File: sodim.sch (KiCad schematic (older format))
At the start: 1 part, among them J1 ddr4-sodimm-edge-connector

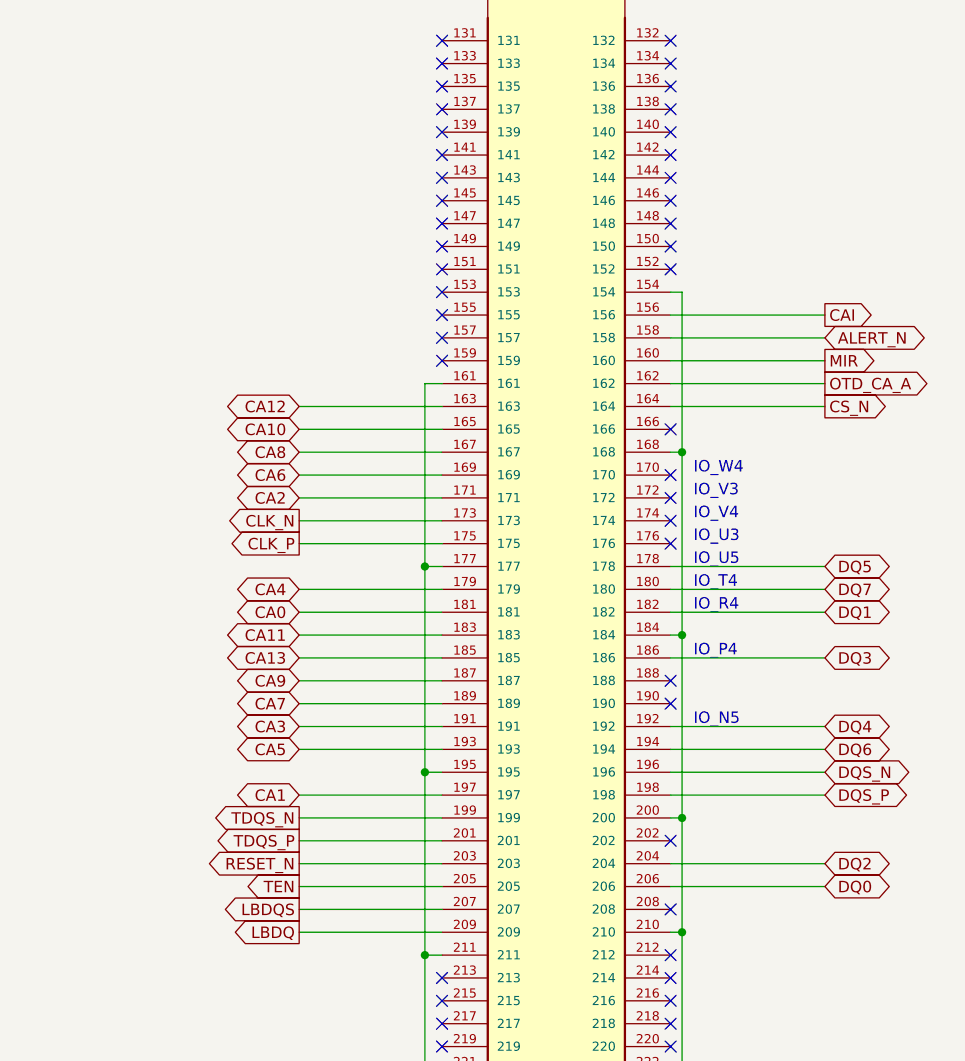
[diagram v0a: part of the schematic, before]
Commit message: Update SODIMM signal assignment
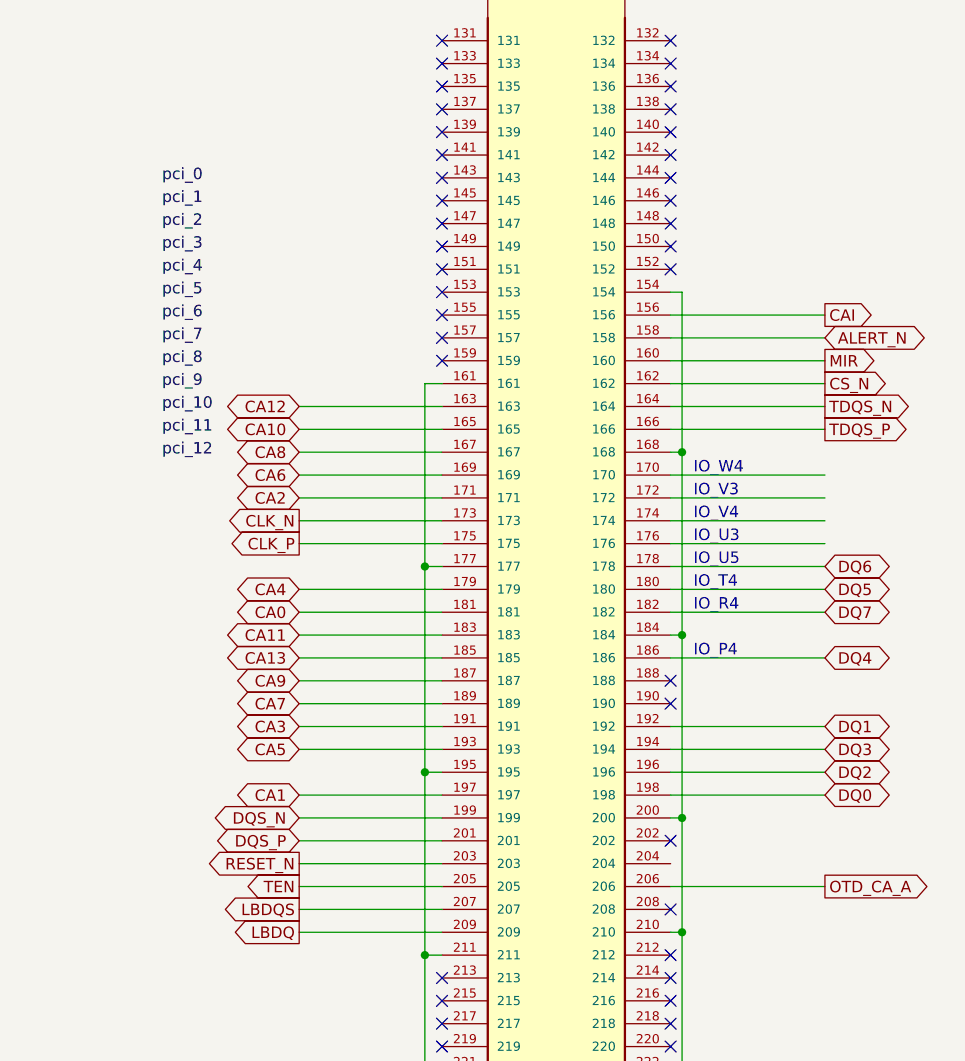
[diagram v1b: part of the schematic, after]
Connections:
- net CS_N: now also J1.162; no longer J1.164
- net DQ0: now also J1.198; no longer J1.206
- net DQ1: now also J1.192; no longer J1.182
- net DQ2: now also J1.196; no longer J1.204
- net DQ3: now also J1.194; no longer J1.186
- net DQ4: now also J1.186; no longer J1.192
- net DQ5: now also J1.180; no longer J1.178
- net DQ6: now also J1.178; no longer J1.194
- net DQ7: now also J1.182; no longer J1.180
- net DQS_N: now also J1.199; no longer J1.196
- net DQS_P: now also J1.201; no longer J1.198
- net OTD_CA_A: now also J1.206; no longer J1.162
- net TDQS_N: now also J1.164; no longer J1.199
- net TDQS_P: now also J1.166; no longer J1.201
- no-connect marks 149 -> 144
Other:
- note removed: "IO_N5"
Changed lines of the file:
@@
 	1    0    0    -1
 $EndComp
-$Comp
-L ddr5-testbed:ddr4-sodimm-edge-connector J1
-U 2 1 600B3548
-P 10000 5800
-AR Path="/5FDC4A05/600B3548" Ref="J1"  Part="2"
-AR Path="/5FF943AC/600B3548" Ref="J?"  Part="2"
-F 0 "J1" H 10000 9365 50  0000 C CNN
-F 1 "ddr4-sodimm-edge-connector" H 10000 9274 50  0000 C CNN
-F 2 "ddr5-testbed-footprints:SODIMM_DDR4_EDGE" H 9700 2400 50  0001 L BNN
-F 3 "" H 11000 5900 50  0001 L BNN
-	2    10000 5800
-	1    0    0    -1
-$EndComp
 Wire Wire Line
 	9500 4200 8875 4200
@@
 	10550 4400 10550 5200
 Wire Wire Line
-	10500 5700 11175 5700
-Wire Wire Line
-	10500 6200 11175 6200
-Wire Wire Line
-	10500 6300 11175 6300
-Wire Wire Line
 	10500 6500 10550 6500
 Connection ~ 10550 6500
@@
 	10500 5200 10550 5200
 Connection ~ 10550 5200
-Wire Wire Line
-	10500 5600 11175 5600
-Wire Wire Line
-	10500 5800 11175 5800
 $Comp
 L ddr5-testbed:GND #PWR0102
@@
 NoConn ~ 10500 5400
 NoConn ~ 10500 5500
-Text Notes 10600 5600 0    50   ~ 0
-IO_N5
 NoConn ~ 10500 6100
 Text GLabel 4075 8800 0    50   BiDi ~ 0
@@
 Wire Wire Line
 	4075 8900 4725 8900
-Text GLabel 11175 5600 2    50   BiDi ~ 0
+Text GLabel 11175 5300 2    50   BiDi ~ 0
 DQ4
-Text GLabel 11175 4900 2    50   BiDi ~ 0
+Text GLabel 11175 5000 2    50   BiDi ~ 0
 DQ5
-Text GLabel 11175 5700 2    50   BiDi ~ 0
+Text GLabel 11175 4900 2    50   BiDi ~ 0
 DQ6
-Text GLabel 11175 5000 2    50   BiDi ~ 0
+Text GLabel 11175 5100 2    50   BiDi ~ 0
 DQ7
-Text GLabel 11175 5300 2    50   BiDi ~ 0
+Text GLabel 11175 5700 2    50   BiDi ~ 0
 DQ3
-Text GLabel 11175 6200 2    50   BiDi ~ 0
+Text GLabel 11175 5800 2    50   BiDi ~ 0
 DQ2
-Text GLabel 11175 5100 2    50   BiDi ~ 0
+Text GLabel 11175 5600 2    50   BiDi ~ 0
 DQ1
-Text GLabel 11175 6300 2    50   BiDi ~ 0
+Text GLabel 11175 5900 2    50   BiDi ~ 0
 DQ0
 Text GLabel 8875 6200 0    50   Output ~ 0
 RESET_N
-Text GLabel 11175 4100 2    50   Output ~ 0
+Text GLabel 11175 6300 2    50   Output ~ 0
 OTD_CA_A
 Text GLabel 8875 6500 0    50   Output ~ 0
@@
 NoConn ~ 10500 8400
 NoConn ~ 10500 8500
-Text GLabel 11175 4200 2    50   Output ~ 0
+Text GLabel 11175 4100 2    50   Output ~ 0
 CS_N
 Text GLabel 8875 5300 0    50   BiDi ~ 0
@@
 Text GLabel 8875 4600 0    50   BiDi ~ 0
 CA2
-Text GLabel 11175 5800 2    50   BiDi ~ 0
+Text GLabel 8875 6000 0    50   BiDi ~ 0
 DQS_N
-Text GLabel 11175 5900 2    50   BiDi ~ 0
+Text GLabel 8875 6100 0    50   BiDi ~ 0
 DQS_P
 Text GLabel 8875 4700 0    50   Output ~ 0
@@
 Text GLabel 8875 4800 0    50   Output ~ 0
 CLK_P
-Text GLabel 8875 6000 0    50   Output ~ 0
+Text GLabel 11175 4200 2    50   Output ~ 0
 TDQS_N
-Text GLabel 8875 6100 0    50   Output ~ 0
+Text GLabel 11175 4300 2    50   Output ~ 0
 TDQS_P
 Wire Wire Line
 	10550 5200 10550 6000
 Wire Wire Line
-	10500 5900 11175 5900
-Wire Wire Line
 	10500 5100 11175 5100
 Wire Wire Line
@@
 Wire Wire Line
 	10500 4900 11175 4900
-NoConn ~ 10500 4500
 Wire Wire Line
 	10500 3800 11175 3800
@@
 Wire Wire Line
 	10500 4100 11175 4100
-NoConn ~ 10500 4300
-NoConn ~ 10500 4600
-NoConn ~ 10500 4700
-NoConn ~ 10500 4800
+Wire Wire Line
+	10500 4700 11175 4700
+Wire Wire Line
+	10500 4800 11175 4800
+Wire Wire Line
+	10500 4500 11175 4500
+Wire Wire Line
+	10500 4600 11175 4600
+$Comp
+L ddr5-testbed:ddr4-sodimm-edge-connector J1
+U 2 1 600B3548
+P 10000 5800
+AR Path="/5FDC4A05/600B3548" Ref="J1"  Part="2"
+AR Path="/5FF943AC/600B3548" Ref="J?"  Part="2"
+F 0 "J1" H 10000 9365 50  0000 C CNN
+F 1 "ddr4-sodimm-edge-connector" H 10000 9274 50  0000 C CNN
+F 2 "ddr5-testbed-footprints:SODIMM_DDR4_EDGE" H 9700 2400 50  0001 L BNN
+F 3 "" H 11000 5900 50  0001 L BNN
+	2    10000 5800
+	1    0    0    -1
+$EndComp
+Wire Wire Line
+	10500 4300 11175 4300
+Wire Wire Line
+	10500 5900 11175 5900
+Wire Wire Line
+	10500 5800 11175 5800
+Wire Wire Line
+	10500 5700 11175 5700
+Wire Wire Line
+	10500 5600 11175 5600
+Wire Wire Line
+	10500 6300 11175 6300
+Text Label 8275 3225 0    50   ~ 0
+pci_0
+Text Label 8275 3325 0    50   ~ 0
+pci_1
+Text Label 8275 3425 0    50   ~ 0
+pci_2
+Text Label 8275 3525 0    50   ~ 0
+pci_3
+Text Label 8275 3625 0    50   ~ 0
+pci_4
+Text Label 8275 3725 0    50   ~ 0
+pci_5
+Text Label 8275 3825 0    50   ~ 0
+pci_6
+Text Label 8275 3925 0    50   ~ 0
+pci_7
+Text Label 8275 4025 0    50   ~ 0
+pci_8
+Text Label 8275 4125 0    50   ~ 0
+pci_9
+Text Label 8275 4225 0    50   ~ 0
+pci_10
+Text Label 8275 4325 0    50   ~ 0
+pci_11
+Text Label 8275 4425 0    50   ~ 0
+pci_12
 $EndSCHEMATC

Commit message: Cleanup
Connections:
- no-connect marks 144 -> 148
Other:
- note removed: "IO_P4"
- note removed: "IO_R4"
- note removed: "IO_T4"
- note removed: "IO_U3"
- note removed: "IO_U5"
- note removed: "IO_V3"
- note removed: "IO_V4"
- note removed: "IO_W4"
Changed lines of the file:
@@
 	1    0    0    -1
 $EndComp
-Text Notes 10600 5300 0    50   ~ 0
-IO_P4
-Text Notes 10600 5100 0    50   ~ 0
-IO_R4
-Text Notes 10600 5000 0    50   ~ 0
-IO_T4
-Text Notes 10600 4900 0    50   ~ 0
-IO_U5
-Text Notes 10600 4800 0    50   ~ 0
-IO_U3
-Text Notes 10600 4700 0    50   ~ 0
-IO_V4
-Text Notes 10600 4600 0    50   ~ 0
-IO_V3
-Text Notes 10600 4500 0    50   ~ 0
-IO_W4
 Wire Wire Line
 	10500 5300 11175 5300
@@
 Wire Wire Line
 	10500 4100 11175 4100
-Wire Wire Line
-	10500 4700 11175 4700
-Wire Wire Line
-	10500 4800 11175 4800
-Wire Wire Line
-	10500 4500 11175 4500
-Wire Wire Line
-	10500 4600 11175 4600
 $Comp
 L ddr5-testbed:ddr4-sodimm-edge-connector J1
@@
 Wire Wire Line
 	10500 6300 11175 6300
-Text Label 8275 3225 0    50   ~ 0
-pci_0
-Text Label 8275 3325 0    50   ~ 0
-pci_1
-Text Label 8275 3425 0    50   ~ 0
-pci_2
-Text Label 8275 3525 0    50   ~ 0
-pci_3
-Text Label 8275 3625 0    50   ~ 0
-pci_4
-Text Label 8275 3725 0    50   ~ 0
-pci_5
-Text Label 8275 3825 0    50   ~ 0
-pci_6
-Text Label 8275 3925 0    50   ~ 0
-pci_7
-Text Label 8275 4025 0    50   ~ 0
-pci_8
-Text Label 8275 4125 0    50   ~ 0
-pci_9
-Text Label 8275 4225 0    50   ~ 0
-pci_10
-Text Label 8275 4325 0    50   ~ 0
-pci_11
-Text Label 8275 4425 0    50   ~ 0
-pci_12
+NoConn ~ 10500 4500
+NoConn ~ 10500 4600
+NoConn ~ 10500 4700
+NoConn ~ 10500 4800
 $EndSCHEMATC

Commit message: Assign schematic labels
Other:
- note added: "Note:\nThe pin assignment for that connector matches\nan experimental research platform available at \nhttps://github.com/antmicro/lpddr4-test-board"
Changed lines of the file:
@@
 Title "DDR5 testbed"
 Date "2022-03-02"
-Rev "1.0.0"
+Rev "1.0.1"
 Comp ""
 Comment1 ""
@@
 NoConn ~ 10500 4700
 NoConn ~ 10500 4800
+Text Notes 925  1700 0    98   ~ 0
+Note:\nThe pin assignment for that connector matches\nan experimental research platform available at \nhttps://github.com/antmicro/lpddr4-test-board
 $EndSCHEMATC
